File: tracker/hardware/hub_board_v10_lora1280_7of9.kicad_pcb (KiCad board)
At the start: 4 copper layers, 72 x 80 mm, 49 parts, among them U1 U1, U2 U2, U3 U3, U5 U5, U6 U6, U7 U7

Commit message: fix(kicad): playbook and all make targets tested end to end -- five real defects found and fixed
The operator hit a hard failure on the very first command (sudo make kicad-setup) and asked that
every target be tested before being handed over. Doing that found five defects, four of them mine.

ANSIBLE (ansible/pcb-workstation.yml) -- the reported failure and two more behind it
  1. REPORTED: gpg: WARNING: nothing exported / "Unable to get required signing key".
     apt_repository: repo=ppa:kicad/... resolves the PPA key over hkp://keyserver.ubuntu.com:80,
     which is blocked here. Fixed by fetching the SAME key over HTTPS into
     /etc/apt/keyrings/kicad.gpg and pinning the repo with signed-by. Proven: the HTTPS lookup
     returns a 2451-byte PGP block; the forced-repo run is ok=18 changed=1 failed=0.
  2. FOUND BEHIND IT: E:Conflicting values set for option Signed-By. A machine that already had
     the PPA carries a source line WITHOUT signed-by, and apt then refuses to read the list at all.
     The playbook now removes stale /etc/apt/sources.list.d/*kicad* before writing its own.
  3. state: latest not present (an installed 7.0.11 satisfies present and nothing is upgraded),
     plus assertions for kicad-cli 9.x, pcbnew under /usr/bin/python3, and /usr/share/kicad/3dmodels.
  4. meshlab + freecad moved behind -e install_extras=true: ~1.5 GB that routing never uses.
  5. New --kicad_force_repo flag, so the repository path can be re-tested on a machine that already
     has KiCad (that is how defect 2 was found at all).

MAKE TARGETS -- all nine exercised, not just written
  kicad-setup      PASS, both paths (idempotent when KiCad 9 is present)
  kicad-verify     PASS. LoRa1280 gate 15 passed; full suite 6 failed / 956 passed, and those 6
                   are PRE-EXISTING: verified red on a pristine origin/master worktree before any
                   change here. The target now hard-gates only the LoRa1280 tests and reports the
                   rest with 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
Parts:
- moved U_LORA1280 1.50 mm to (53.0, 68.1)
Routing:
- net /E28_DIO2: track 74.4 -> 51.8 mm, vias 0 -> 2
- net /SPI1_MOSI: track 63.6 -> 73.1 mm
- net /E28_BUSY: track 51.4 -> 53.0 mm
- net /E28_DIO1: track 72.8 -> 74.4 mm
- net /SPI1_MISO: track 179.7 -> 181.2 mm
- net /E28_RESET_N: track 69.9 -> 71.4 mm, vias 2 -> 4
- net /E28_CS_N: track 69.4 -> 69.9 mm

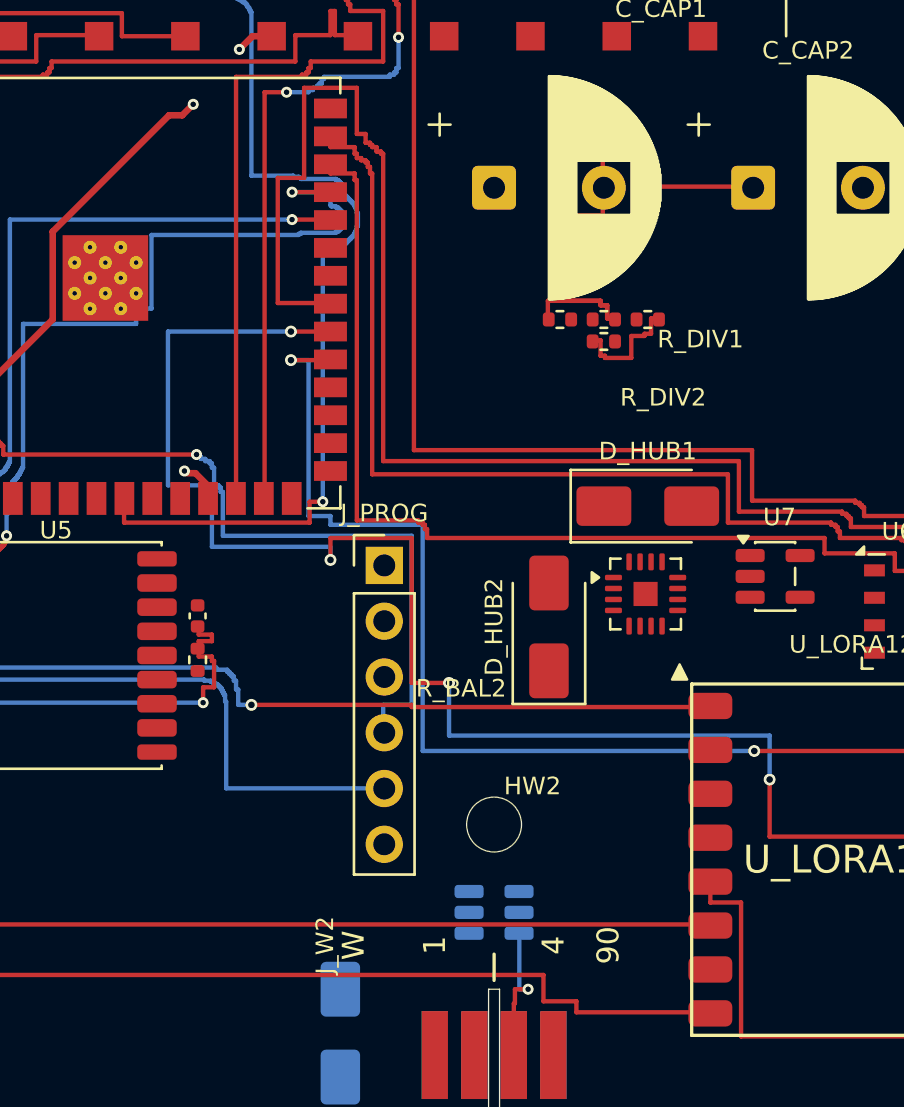
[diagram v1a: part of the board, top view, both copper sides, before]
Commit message: route(hub): finish SPI1_SCK and E28_DIO3 for the LoRa1280 site
Routed both remaining LoRa1280 interface nets by hand and moved the lanes
that blocked them. No design-rule relaxation: 0.20 mm clearance, 0.24 mm
trace, 0.50 mm via, 0.30 mm drill.
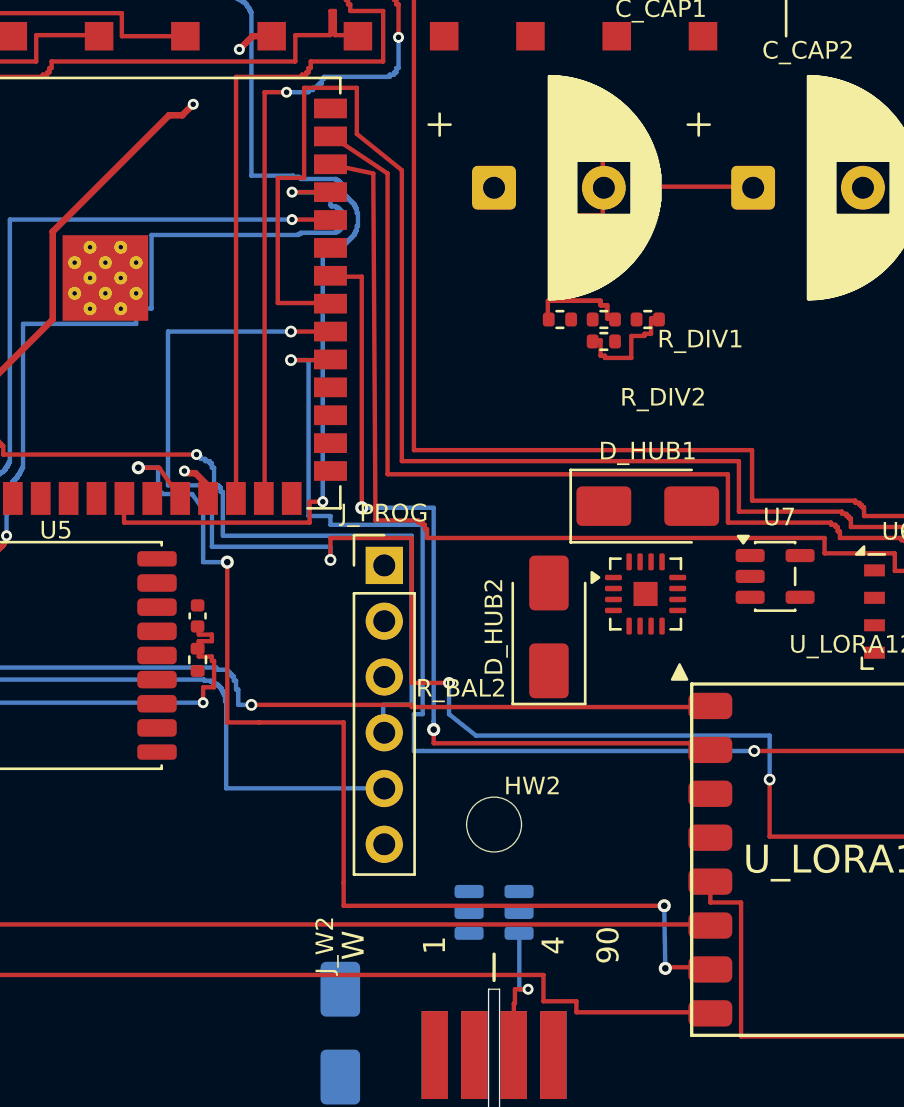
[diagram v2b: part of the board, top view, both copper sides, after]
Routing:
- net /I2C_SCL: track 45.4 -> 27.2 mm
- net /E28_RESET_N: track 71.4 -> 54.4 mm
- net /E28_DIO1: track 74.4 -> 57.4 mm
- net /E28_BUSY: track 53.0 -> 42.7 mm
- net /I2C_SDA: track 49.7 -> 45.4 mm
- net /SPI1_SCK: vias 0 -> 4
- net /E28_DIO3: vias 0 -> 2
